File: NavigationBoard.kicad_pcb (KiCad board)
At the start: 2 copper layers, 50 x 45 mm, 31 parts, among them J1 Conn_01x03, J2 Conn_01x03, J3 Conn_01x03, J4 Conn_01x03, J5 USB_C_Receptacle_USB2.0, U1 ATmega2560-16AU, U2 RFM96W-433S2, U3 FT230XQ, U4 MPL115A1, U5 L86

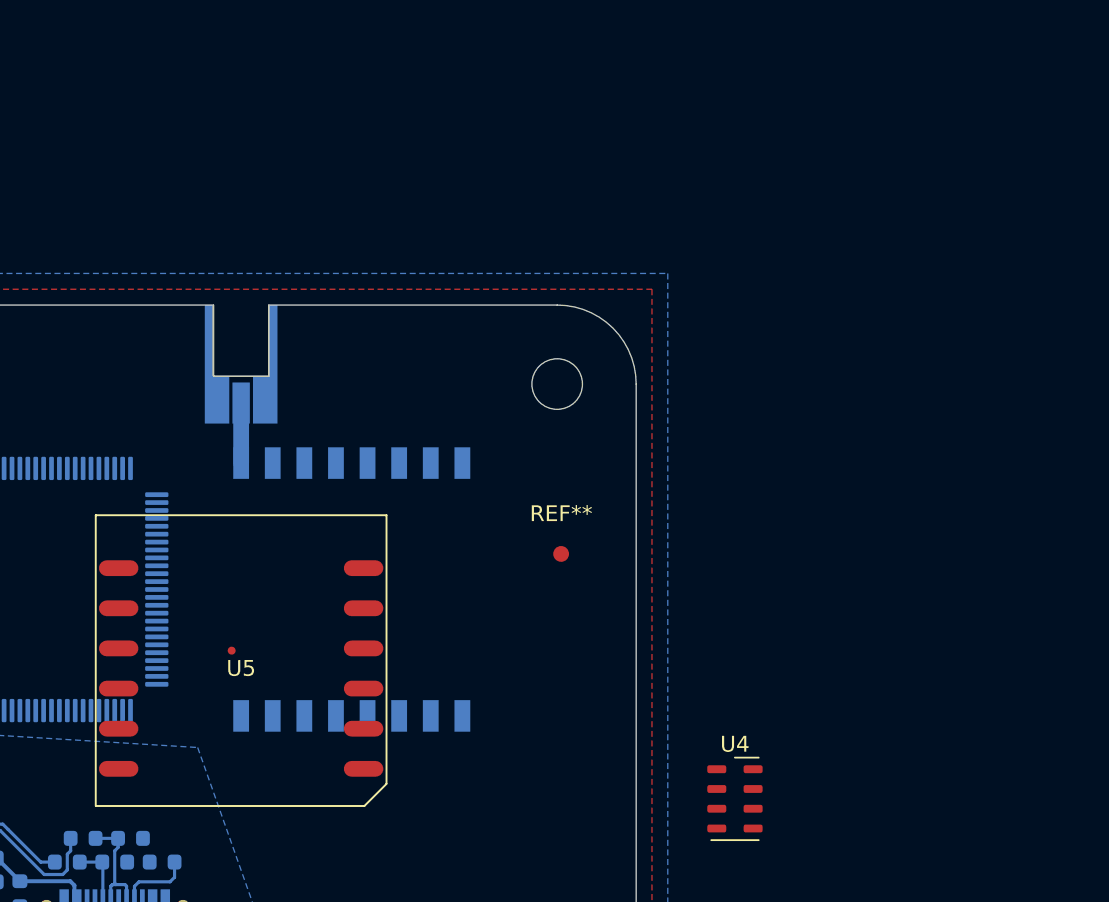
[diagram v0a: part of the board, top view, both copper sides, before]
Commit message: 3V regulator, crystal oscillator, reset switch, new GPS
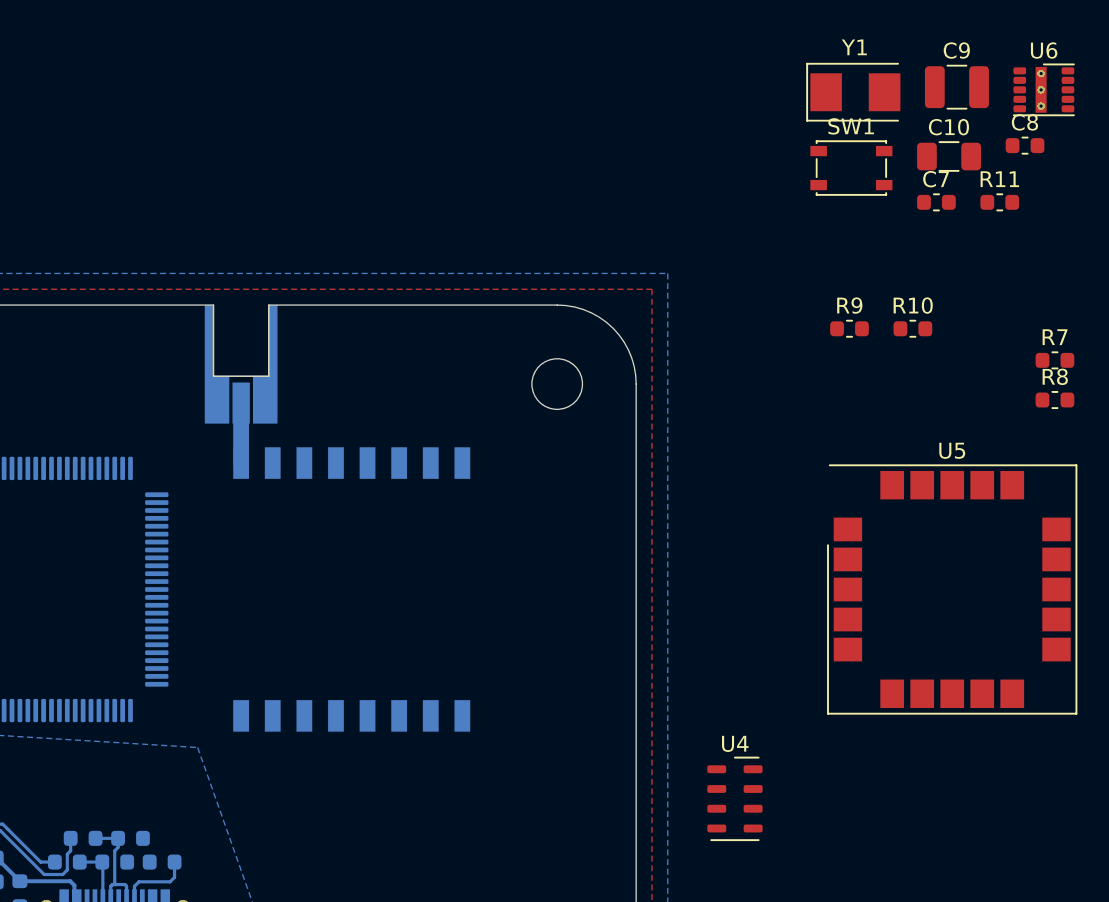
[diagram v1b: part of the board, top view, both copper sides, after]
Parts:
- removed REF**: Fiducial_1mm_Mask3mm, Fiducial:Fiducial_1mm_Mask3mm
- added C10: 22µF, Capacitor_SMD:C_1206_3216Metric, F.Cu at (69.8, -9.40)
- added C7: 8pF, Capacitor_SMD:C_0603_1608Metric, F.Cu at (69.0, -6.50)
- added C8: 8pF, Capacitor_SMD:C_0603_1608Metric, F.Cu at (74.6, -10.1)
- added C9: 10µF, Capacitor_SMD:C_1210_3225Metric, F.Cu at (70.3, -13.8)
- added R10: 10k, Resistor_SMD:R_0603_1608Metric, F.Cu at (67.5, 1.50)
- added R11: 10k, Resistor_SMD:R_0603_1608Metric, F.Cu at (73.0, -6.50)
- added R7: 10k, Resistor_SMD:R_0603_1608Metric, F.Cu at (76.5, 3.50)
- added R8: 10k, Resistor_SMD:R_0603_1608Metric, F.Cu at (76.5, 6.01)
- added R9: 10k, Resistor_SMD:R_0603_1608Metric, F.Cu at (63.5, 1.50)
- added SW1: SW_Push, Button_Switch_SMD:SW_SPST_PTS810, F.Cu at (63.6, -8.67)
- added U6: LMZM23600V3, Package_LGA:Texas_SIL0010A_MicroSiP-10-1EP_3.8x3mm_P0.6mm_EP0.7x2.9mm_ThermalVias, F.Cu at (75.8, -13.6)
- added Y1: 16MHz, Crystal:Crystal_SMD_5032-2Pin_5.0x3.2mm, F.Cu at (63.9, -13.5)
- U5: value L86 -> ublox_SAM-M8Q; footprint GPS:L86 -> RF_GPS:ublox_SAM-M8Q
- moved U5 45.2 mm to (70.0, 18.0)
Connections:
- net /FT230/5VOUT renamed +5V
- J1 pad 1: (no net) -> Net-(J1-Pad1)
- J1 pad 2: (no net) -> Net-(J1-Pad2)
- J1 pad 3: (no net) -> Net-(J1-Pad3)
- J2 pad 1: (no net) -> Net-(J2-Pad1)
- J2 pad 2: (no net) -> Net-(J2-Pad2)
- J2 pad 3: (no net) -> Net-(J2-Pad3)
- J3 pad 1: (no net) -> Net-(J3-Pad1)
- J3 pad 2: (no net) -> Net-(J3-Pad2)
- J3 pad 3: (no net) -> Net-(J3-Pad3)
- J4 pad 1: (no net) -> Net-(J4-Pad1)
- J4 pad 2: (no net) -> Net-(J4-Pad2)
- J4 pad 3: (no net) -> Net-(J4-Pad3)
- J5 pad A8: (no net) -> Net-(J5-PadA8)
- J5 pad B8: (no net) -> Net-(J5-PadB8)
- U1 pad 1: (no net) -> Net-(U1-Pad1)
- U1 pad 12: (no net) -> /RXD2
- U1 pad 13: (no net) -> /TXD2
- U1 pad 14: (no net) -> Net-(U1-Pad14)
- U1 pad 15: (no net) -> Net-(U1-Pad15)
- U1 pad 16: (no net) -> Net-(U1-Pad16)
- U1 pad 17: (no net) -> Net-(U1-Pad17)
- U1 pad 18: (no net) -> Net-(U1-Pad18)
- U1 pad 23: (no net) -> Net-(U1-Pad23)
- U1 pad 24: (no net) -> Net-(U1-Pad24)
- U1 pad 25: (no net) -> Net-(U1-Pad25)
- U1 pad 26: (no net) -> Net-(U1-Pad26)
- U1 pad 27: (no net) -> Net-(U1-Pad27)
- U1 pad 28: (no net) -> Net-(U1-Pad28)
- U1 pad 29: (no net) -> Net-(U1-Pad29)
- U1 pad 30: (no net) -> /~RESET
- U1 pad 33: (no net) -> Net-(C8-Pad1)
- U1 pad 34: (no net) -> Net-(C7-Pad1)
- U1 pad 35: (no net) -> Net-(U1-Pad35)
- U1 pad 36: (no net) -> Net-(U1-Pad36)
- U1 pad 37: (no net) -> Net-(U1-Pad37)
- U1 pad 38: (no net) -> Net-(U1-Pad38)
- U1 pad 39: (no net) -> Net-(U1-Pad39)
- U1 pad 4: (no net) -> Net-(U1-Pad4)
- U1 pad 40: (no net) -> Net-(U1-Pad40)
- U1 pad 41: (no net) -> Net-(U1-Pad41)
- U1 pad 42: (no net) -> Net-(U1-Pad42)
- U1 pad 43: (no net) -> Net-(U1-Pad43)
- U1 pad 44: (no net) -> Net-(U1-Pad44)
- U1 pad 45: (no net) -> Net-(U1-Pad45)
- U1 pad 46: (no net) -> Net-(U1-Pad46)
- U1 pad 47: (no net) -> Net-(U1-Pad47)
- U1 pad 48: (no net) -> Net-(U1-Pad48)
- U1 pad 49: (no net) -> Net-(U1-Pad49)
- U1 pad 5: (no net) -> Net-(U1-Pad5)
- U1 pad 50: (no net) -> Net-(U1-Pad50)
- U1 pad 51: (no net) -> Net-(U1-Pad51)
- U1 pad 52: (no net) -> Net-(U1-Pad52)
- U1 pad 53: (no net) -> Net-(U1-Pad53)
- U1 pad 54: (no net) -> Net-(U1-Pad54)
- U1 pad 55: (no net) -> Net-(U1-Pad55)
- U1 pad 56: (no net) -> Net-(U1-Pad56)
- U1 pad 57: (no net) -> Net-(U1-Pad57)
- U1 pad 58: (no net) -> Net-(U1-Pad58)
- U1 pad 59: (no net) -> Net-(U1-Pad59)
- U1 pad 6: (no net) -> Net-(U1-Pad6)
- U1 pad 60: (no net) -> Net-(U1-Pad60)
- U1 pad 63: (no net) -> Net-(U1-Pad63)
- U1 pad 64: (no net) -> Net-(U1-Pad64)
- U1 pad 65: (no net) -> Net-(U1-Pad65)
- U1 pad 66: (no net) -> Net-(U1-Pad66)
- U1 pad 67: (no net) -> Net-(U1-Pad67)
- U1 pad 68: (no net) -> Net-(U1-Pad68)
- U1 pad 69: (no net) -> Net-(U1-Pad69)
- U1 pad 7: (no net) -> Net-(U1-Pad7)
- U1 pad 70: (no net) -> Net-(U1-Pad70)
- U1 pad 71: (no net) -> Net-(U1-Pad71)
- U1 pad 72: (no net) -> Net-(U1-Pad72)
- U1 pad 73: (no net) -> Net-(U1-Pad73)
- U1 pad 74: (no net) -> Net-(U1-Pad74)
- U1 pad 75: (no net) -> Net-(U1-Pad75)
- U1 pad 76: (no net) -> Net-(U1-Pad76)
- U1 pad 77: (no net) -> Net-(U1-Pad77)
- U1 pad 78: (no net) -> Net-(U1-Pad78)
- U1 pad 79: (no net) -> Net-(U1-Pad79)
- U1 pad 8: (no net) -> Net-(U1-Pad8)
- U1 pad 82: (no net) -> Net-(U1-Pad82)
- U1 pad 83: (no net) -> Net-(U1-Pad83)
- U1 pad 84: (no net) -> Net-(U1-Pad84)
- U1 pad 85: (no net) -> Net-(U1-Pad85)
- U1 pad 86: (no net) -> Net-(U1-Pad86)
- U1 pad 87: (no net) -> Net-(U1-Pad87)
- U1 pad 88: (no net) -> Net-(U1-Pad88)
- U1 pad 89: (no net) -> Net-(U1-Pad89)
- U1 pad 9: (no net) -> Net-(U1-Pad9)
- U1 pad 90: (no net) -> Net-(U1-Pad90)
- U1 pad 91: (no net) -> Net-(U1-Pad91)
- U1 pad 92: (no net) -> Net-(U1-Pad92)
- U1 pad 93: (no net) -> Net-(U1-Pad93)
- U1 pad 94: (no net) -> Net-(U1-Pad94)
- U1 pad 95: (no net) -> Net-(U1-Pad95)
- U1 pad 96: (no net) -> Net-(U1-Pad96)
- U1 pad 97: (no net) -> Net-(U1-Pad97)
- U1 pad 98: (no net) -> +3V3
- U2 pad 11: (no net) -> Net-(U2-Pad11)
- U2 pad 12: (no net) -> Net-(U2-Pad12)
- U2 pad 14: (no net) -> Net-(U2-Pad14)
- U2 pad 15: (no net) -> Net-(U2-Pad15)
- U2 pad 16: (no net) -> Net-(U2-Pad16)
- U2 pad 6: (no net) -> Net-(U2-Pad6)
- U2 pad 7: (no net) -> Net-(U2-Pad7)
- U3 pad 12: (no net) -> Net-(U3-Pad12)
- U3 pad 14: (no net) -> Net-(U3-Pad14)
- U3 pad 15: (no net) -> /RXD0
- U3 pad 16: (no net) -> Net-(U3-Pad16)
- U3 pad 2: (no net) -> /TXD0
- U3 pad 4: (no net) -> Net-(U3-Pad4)
- U4 pad 1: (no net) -> Net-(U4-Pad1)
- U4 pad 2: (no net) -> Net-(U4-Pad2)
- U4 pad 3: (no net) -> Net-(U4-Pad3)
- U4 pad 4: (no net) -> Net-(U4-Pad4)
- U4 pad 5: (no net) -> Net-(U4-Pad5)
- U4 pad 6: (no net) -> Net-(U4-Pad6)
- U4 pad 7: (no net) -> Net-(U4-Pad7)
- U4 pad 8: (no net) -> Net-(U4-Pad8)
- U5 pad 1: /TXD0 -> GND
- U5 pad 10: (no net) -> GND
- U5 pad 11: (no net) -> GND
- U5 pad 12: GND -> Net-(U5-Pad12)
- U5 pad 2: /RXD0 -> +3V3
- U5 pad 3: GND -> +3V3
- U5 pad 4: +3V3 -> GND
- U5 pad 5: +3V3 -> GND
- U5 pad 6: (no net) -> GND
- U5 pad 7: (no net) -> Net-(U5-Pad7)
- U5 pad 8: (no net) -> Net-(U5-Pad8)
- U5 pad 9: (no net) -> Net-(U5-Pad9)

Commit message: add ISP, MPL3115A2
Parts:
- added J6: AVR-ISP-6, Connector_IDC:IDC-Header_2x03_P2.54mm_Vertical, F.Cu at (85.0, 18.0)
- U4: value MPL115A1 -> MPL3115A2; footprint Package_LGA:NXP_MPL115A1_LGA-8_3x5mm_P1.25mm -> Package_LGA:NXP_LGA-8_3x5mm_P1.25mm_H1.1mm
- moved U4 14.5 mm to (70.0, 35.8)

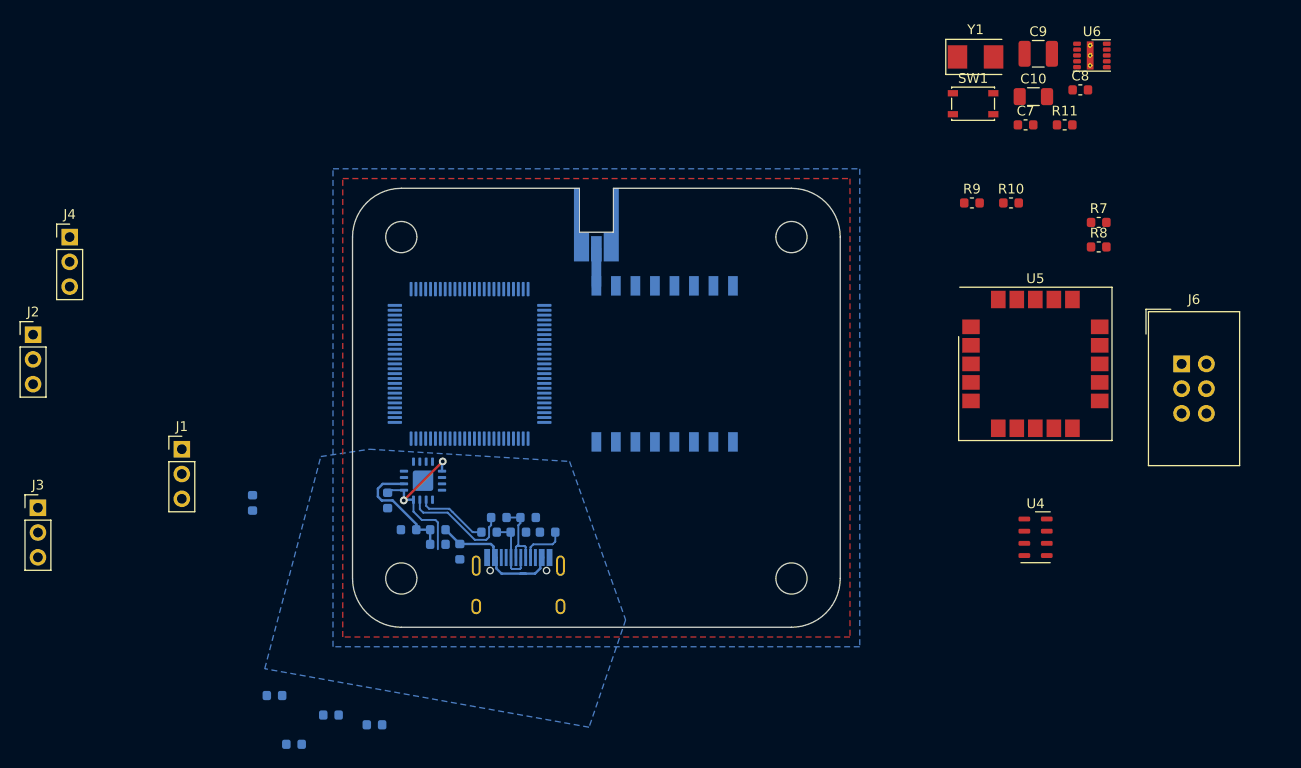
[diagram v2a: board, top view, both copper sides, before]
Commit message: no clue, this has been >4 months and diff is kinda useless here...
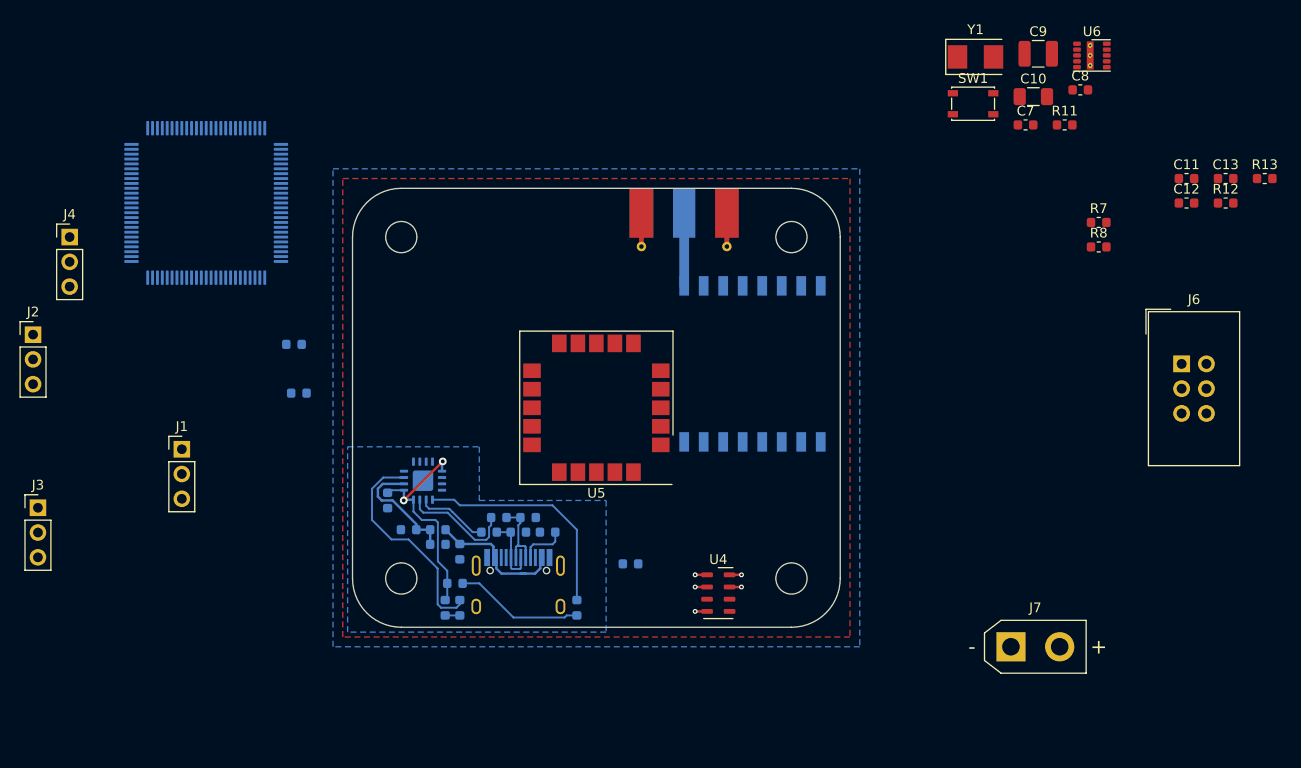
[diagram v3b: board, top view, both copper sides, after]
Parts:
- added C11: 10µF, Capacitor_SMD:C_0603_1608Metric, F.Cu at (85.5, -1.00)
- added C12: 100nF, Capacitor_SMD:C_0603_1608Metric, F.Cu at (85.5, 1.51)
- added C13: 100nF, Capacitor_SMD:C_0603_1608Metric, F.Cu at (89.5, -1.00)
- added J7: Conn_01x02, Connector_AMASS:AMASS_XT30UPB-M_1x02_P5.0mm_Vertical, F.Cu at (67.5, 47.0)
- added R12: 10k, Resistor_SMD:R_0603_1608Metric, F.Cu at (89.5, 1.51)
- added R13: 10k, Resistor_SMD:R_0603_1608Metric, F.Cu at (93.5, -1.00)
- AE1: footprint Connector_Coaxial:MMCX_Molex_73415-0961_Horizontal_1.6mm-PCB -> Connector_Coaxial:SMA_Molex_73251-1153_EdgeMount_Horizontal
- R10, R9: moved to B.Cu
- moved R10 75.6 mm to (-5.50, 21.0), turned to 180 degrees
- moved R9 71.0 mm to (-6.00, 16.0), turned to 180 degrees
- moved U5 45.2 mm to (25.0, 22.5), turned to 180 degrees
- moved R2 39.3 mm to (28.5, 38.5), turned to 0 degrees
- moved U4 33.0 mm to (37.5, 41.5)
- moved U1 31.6 mm to (-15.0, 1.50)
- moved D2 27.5 mm to (23.0, 43.0), turned to 270 degrees
- moved R6 21.8 mm to (10.5, 40.5)
- moved R5 20.9 mm to (9.50, 43.0), turned to 270 degrees
- moved D1 14.9 mm to (11.0, 43.0), turned to 270 degrees
- moved AE1 9.01 mm to (34.0, 4.25)
- moved U2 9.00 mm to (41.0, 18.0)
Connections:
- C10 pad 2: Net-(C10-Pad2) -> GND
- C9 pad 2: Net-(C10-Pad2) -> GND
- U1 pad 43: Net-(U1-Pad43) -> /SCL
- U1 pad 44: Net-(U1-Pad44) -> /SDA
- U4 pad 1: Net-(U4-Pad1) -> +3V3
- U4 pad 3: Net-(U4-Pad3) -> GND
- U4 pad 4: Net-(U4-Pad4) -> +3V3
- U4 pad 7: Net-(U4-Pad7) -> /SDA
- U4 pad 8: Net-(U4-Pad8) -> /SCL
- U6 pad 1: Net-(C10-Pad2) -> GND
- U6 pad 11: Net-(C10-Pad2) -> GND
- U6 pad 2: Net-(C10-Pad2) -> GND
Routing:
- net Net-(D2-Pad1): track 0.00 -> 23.3 mm
- net Net-(D1-Pad1): track 0.00 -> 22.4 mm
- net Net-(D2-Pad2): track 0.00 -> 13.3 mm
- net Net-(C6-Pad1): track 17.3 -> 23.0 mm
- net Net-(AE1-Pad1): track 3.80 -> 7.47 mm
- net +3V3: track 0.00 -> 2.45 mm, vias 0 -> 2
- net Net-(D1-Pad2): track 0.00 -> 1.50 mm
- net Net-(C12-Pad2): track 0.00 -> 1.23 mm, vias 0 -> 1
- net /SDA: track 0.00 -> 1.23 mm, vias 0 -> 1
- net /SCL: track 0.00 -> 1.23 mm, vias 0 -> 1
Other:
- outline, holes or cut-outs redrawn

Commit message: Erster Grober Entwurf
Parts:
- C10, C11, C12, C13, C7, C8, C9, R12, R13, R7, R8, U4, U6, Y1: moved to B.Cu
- moved U6 81.9 mm to (3.00, 24.0), turned to 180 degrees
- moved R11 79.2 mm to (1.50, 27.5), turned to 90 degrees
- moved R13 73.0 mm to (29.5, 34.0), turned to 90 degrees
- moved J7 70.5 mm to (3.50, 17.5), turned to 90 degrees
- moved C10 70.5 mm to (7.50, 23.5), turned to 270 degrees
- moved R12 70.0 mm to (27.5, 34.0), turned to 90 degrees
- moved SW1 68.2 mm to (3.50, 23.5)
- moved C13 66.0 mm to (33.5, 34.0), turned to 270 degrees
- moved C11 64.4 mm to (31.5, 34.0), turned to 270 degrees
- moved C9 60.8 mm to (12.0, 3.50), turned to 90 degrees
- moved R7 60.5 mm to (16.0, 2.50), turned to 270 degrees
- moved R8 58.1 mm to (18.5, 2.50), turned to 270 degrees
- moved C12 54.9 mm to (38.0, 29.0)
- moved J6 53.8 mm to (35.5, 39.0), turned to 270 degrees
- moved C8 49.1 mm to (29.0, 8.00)
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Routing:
- net +3V3: track 2.45 -> 196.9 mm, vias 2 -> 6
- net /SCK: track 0.00 -> 79.2 mm, vias 0 -> 3
- net /MOSI: track 0.00 -> 77.5 mm, vias 0 -> 3
- net /MISO: track 0.00 -> 69.6 mm, vias 0 -> 3
- net /~RESET: track 0.00 -> 64.4 mm, vias 0 -> 1
- net /~SS: track 0.00 -> 50.3 mm, vias 0 -> 2
- net +5V: track 12.3 -> 51.0 mm, vias 0 -> 2
- net /TXD0: track 0.00 -> 31.9 mm
- net /RXD0: track 0.00 -> 29.3 mm
- net /TXD2: track 0.00 -> 28.1 mm, vias 0 -> 1
- net /SDA: track 1.23 -> 28.4 mm, vias 1 -> 0
- net Net-(J5-PadB5): track 0.00 -> 27.1 mm, vias 0 -> 2
- net /SCL: track 1.23 -> 26.5 mm, vias 1 -> 0
- net /RXD2: track 0.00 -> 23.2 mm, vias 0 -> 1
- net Net-(C8-Pad1): track 0.00 -> 7.80 mm
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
